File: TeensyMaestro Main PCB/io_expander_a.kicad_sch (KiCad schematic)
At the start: 29 parts, among them J1 Male Connector, J2 B5B-XH-A_LF__SN_, SW1 RotaryEncoder_Powered, SW2 PEC11L-4120F-S0020, SW3 PEC11L-4120F-S0020, SW4 PEC11L-4120F-S0020, SW5 PEC11L-4120F-S0020, U4 MCP23008-xP

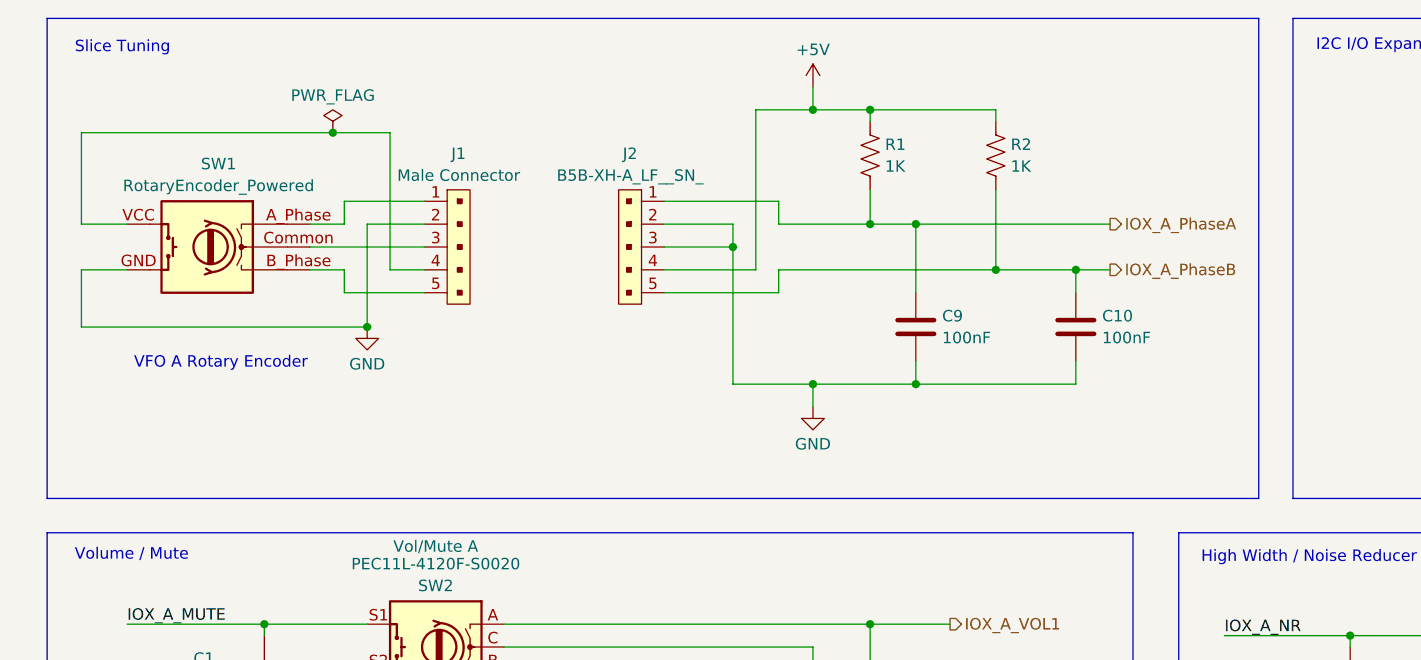
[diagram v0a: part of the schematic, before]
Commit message: Updated documentation in schematic
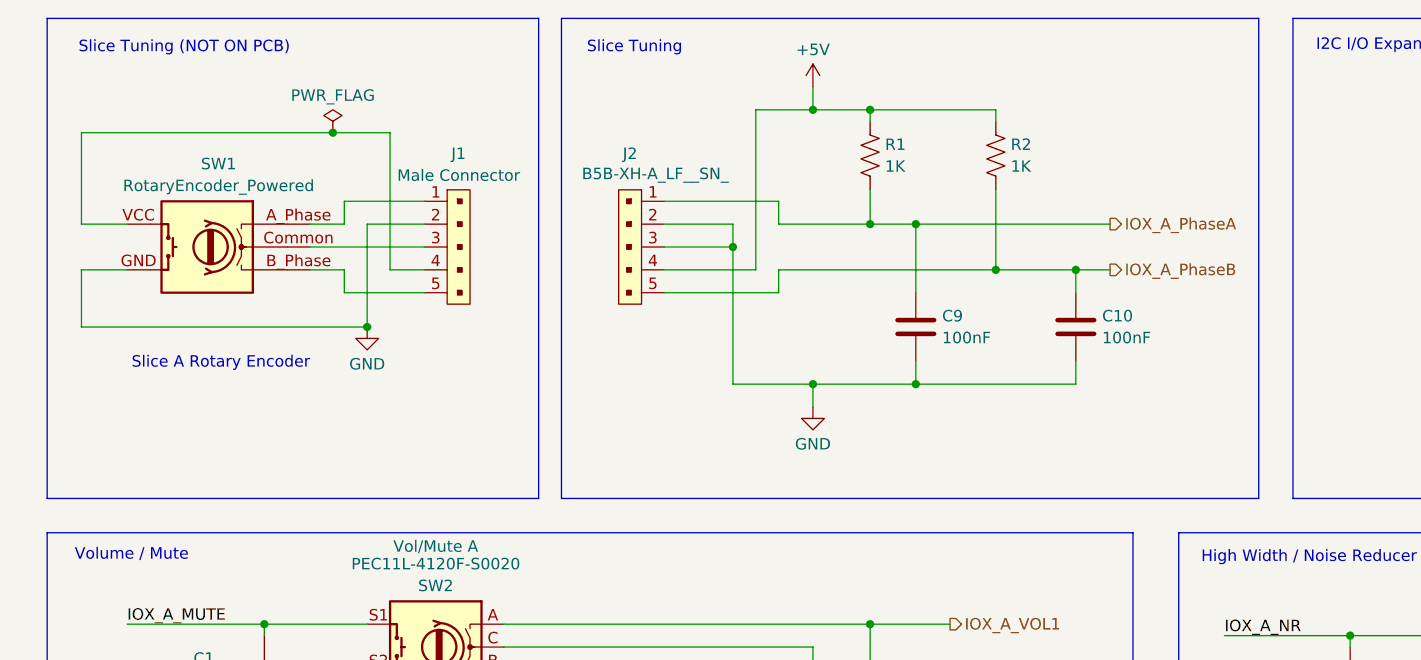
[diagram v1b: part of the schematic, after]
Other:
- note added: "Slice A Rotary Encoder"
- note added: "Slice Tuning (NOT ON PCB)"
- note removed: "VFO A Rotary Encoder"
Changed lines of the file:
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@@
 	)
 	(rectangle
+		(start 17.78 15.24)
+		(end 72.39 68.58)
+		(stroke
+			(width 0)
+			(type default)
+		)
+		(fill
+			(type none)
+		)
+	)
+	(rectangle
 		(start 17.78 113.03)
 		(end 137.16 151.13)
@@
 	)
 	(rectangle
-		(start 17.78 15.24)
+		(start 74.93 15.24)
 		(end 152.4 68.58)
 		(stroke
@@
 		)
 	)
+	(text "Slice Tuning (NOT ON PCB)"
+		(exclude_from_sim no)
+		(at 33.02 18.542 0)
+		(effects
+			(font
+				(size 1.27 1.27)
+			)
+		)
+	)
 	(text "Slice Tuning"
 		(exclude_from_sim no)
-		(at 26.162 18.542 0)
+		(at 83.058 18.542 0)
 		(effects
 			(font
@@
 		)
 	)
-	(text "VFO A Rotary Encoder"
+	(text "Slice A Rotary Encoder"
 		(exclude_from_sim no)
 		(at 37.084 53.594 0)
@@
 		(on_board yes)
 		(dnp no)
-		(fields_autoplaced yes)
 		(property "Reference" "J2"
 			(at 82.55 30.2725 90)
@@
 		)
 		(property "Value" "B5B-XH-A_LF__SN_"
-			(at 82.55 32.6968 90)
+			(at 85.344 32.512 90)
 			(effects
 				(font

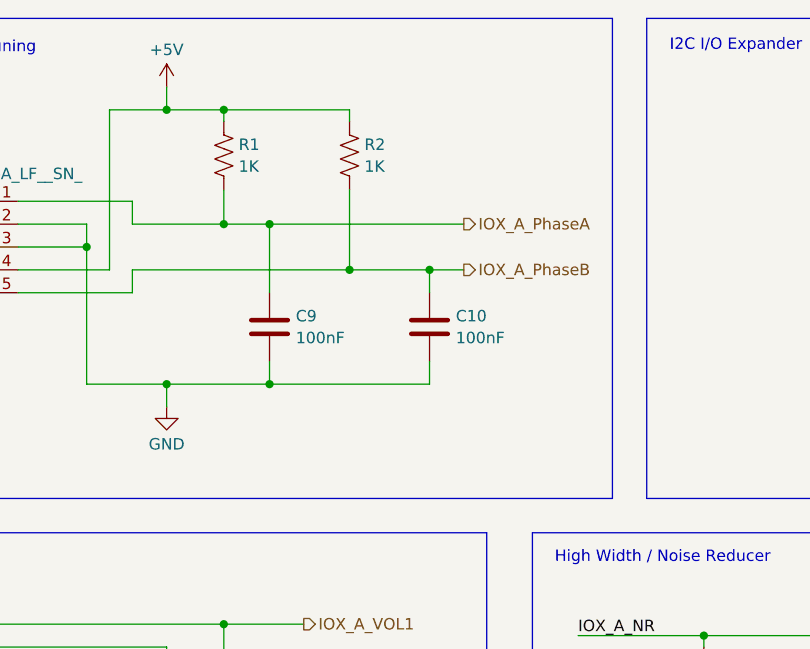
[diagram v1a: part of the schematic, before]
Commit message: Update schematic with 5v pullup correction
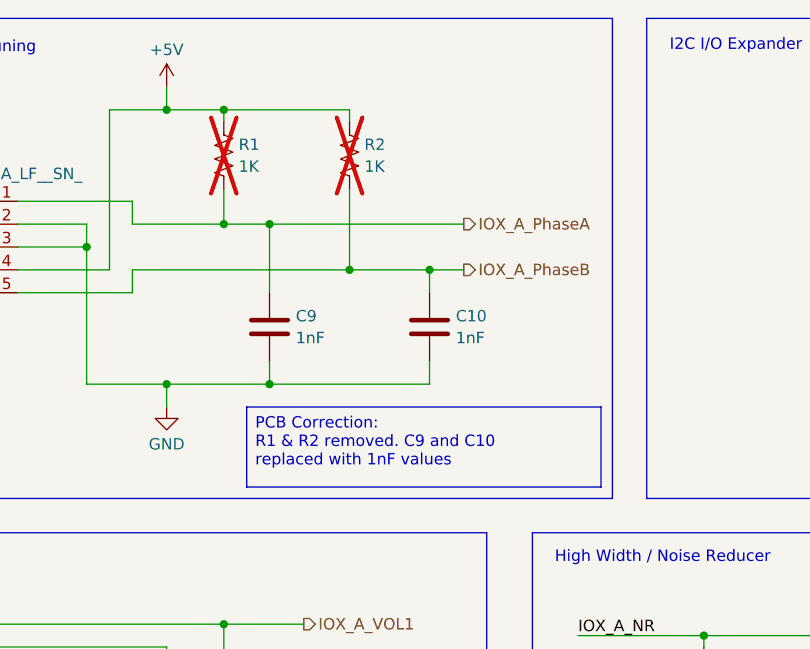
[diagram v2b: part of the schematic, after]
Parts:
- C10, C9: value 100nF -> 1nF
- R1, R2: now not fitted; now left out of the parts list
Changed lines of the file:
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@@
 		)
 	)
+	(text_box "PCB Correction:\nR1 & R2 removed. C9 and C10 replaced with 1nF values"
+		(exclude_from_sim no)
+		(at 111.76 58.42 0)
+		(size 39.37 8.89)
+		(margins 0.9525 0.9525 0.9525 0.9525)
+		(stroke
+			(width 0)
+			(type solid)
+		)
+		(fill
+			(type none)
+		)
+		(effects
+			(font
+				(size 1.27 1.27)
+			)
+			(justify left top)
+		)
+	)
 	(text_box "I2C Address: 0x20\nI2C clock speed: 400 KHz"
 		(exclude_from_sim no)
@@
 		(at 109.22 30.48 0)
 		(unit 1)
-		(exclude_from_sim no)
-		(in_bom yes)
+		(exclude_from_sim yes)
+		(in_bom no)
 		(on_board yes)
-		(dnp no)
+		(dnp yes)
 		(fields_autoplaced yes)
 		(property "Reference" "R1"
@@
 		(at 123.19 30.48 0)
 		(unit 1)
-		(exclude_from_sim no)
-		(in_bom yes)
+		(exclude_from_sim yes)
+		(in_bom no)
 		(on_board yes)
-		(dnp no)
+		(dnp yes)
 		(fields_autoplaced yes)
 		(property "Reference" "R2"
@@
 			)
 		)
-		(property "Value" "100nF"
+		(property "Value" "1nF"
 			(at 117.221 50.7421 0)
 			(effects
@@
 			)
 		)
-		(property "Value" "100nF"
+		(property "Value" "1nF"
 			(at 135.001 50.7421 0)
 			(effects
